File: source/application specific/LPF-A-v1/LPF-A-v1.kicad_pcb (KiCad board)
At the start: 6 copper layers, 32 x 20 mm, 33 parts, among them J1 Conn_01x01_Pin, J2 Conn_01x01_Pin, J3 Conn_01x01_Pin, J4 Conn_01x01_Pin, J5 Conn_01x01_Pin, J6 Conn_01x01_Pin, J7 Conn_01x01_Pin, U1 OPA140, U2 OPA140

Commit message: Updates
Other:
- board text added: "The Manhattan Toolkit LPF-A-v1"
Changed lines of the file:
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@@
 		(layer "Edge.Cuts")
+	)
+	(gr_text "The Manhattan Toolkit\nLPF-A-v1"
+		(at 150 110.25 0)
+		(layer "B.SilkS")
+		(effects
+			(font
+				(size 0.8 0.8)
+				(thickness 0.15)
+				(bold yes)
+			)
+			(justify mirror)
+		)
 	)
 	(gr_text "0V"

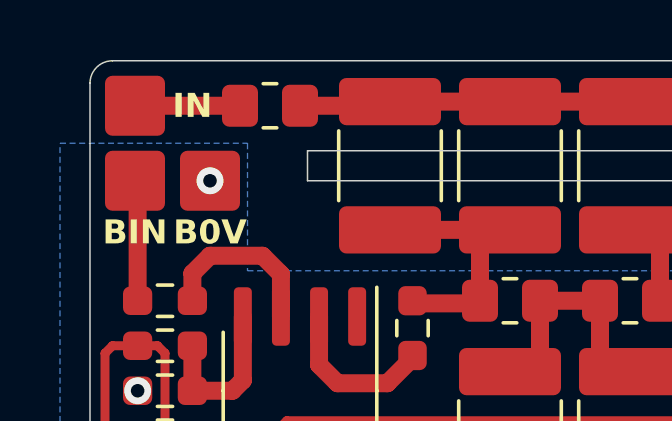
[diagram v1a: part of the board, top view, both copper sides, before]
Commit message: Switched 0805 resistor to 1206
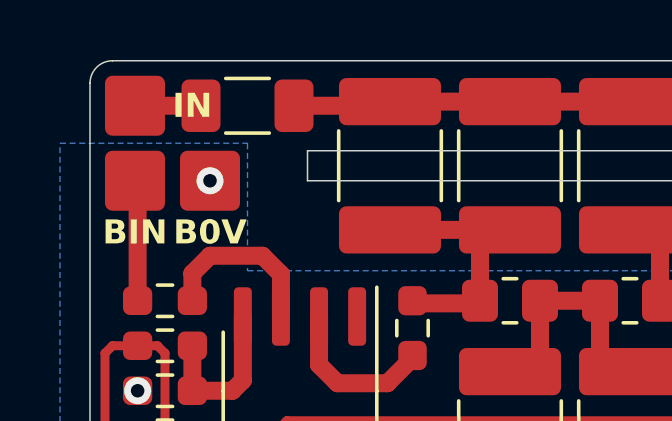
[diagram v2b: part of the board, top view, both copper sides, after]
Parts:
- C7, C8: value 47n -> 10n
- R1: footprint Resistor_SMD:R_0805_2012Metric_Pad1.20x1.40mm_HandSolder -> Resistor_SMD:R_1206_3216Metric_Pad1.30x1.75mm_HandSolder
- R7: value 1k -> 2.2k
- R8: value 100 -> 220
- moved R1 0.75 mm to (139.2, 101.5)
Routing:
- net In: track 3.50 -> 2.20 mm
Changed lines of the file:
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@@
 			)
 		)
-		(property "Value" "47n"
+		(property "Value" "10n"
 			(at 0 1.43 0)
 			(layer "F.Fab")
@@
 			)
 		)
-		(property "Value" "100"
+		(property "Value" "220"
 			(at 0 1.43 0)
 			(layer "F.Fab")
@@
 		)
 	)
-	(footprint "Resistor_SMD:R_0805_2012Metric_Pad1.20x1.40mm_HandSolder"
+	(footprint "Resistor_SMD:R_1206_3216Metric_Pad1.30x1.75mm_HandSolder"
 		(layer "F.Cu")
-		(at 140 101.5)
-		(descr "Resistor SMD 0805 (2012 Metric), square (rectangular) end terminal, IPC_7351 nominal with elongated pad for handsoldering. (Body size source: IPC-SM-782 page 72, https://www.pcb-3d.com/wordpress/wp-content/uploads/ipc-sm-782a_amendment_1_and_2.pdf), generated with kicad-footprint-generator")
+		(at 139.25 101.5)
+		(descr "Resistor SMD 1206 (3216 Metric), square (rectangular) end terminal, IPC_7351 nominal with elongated pad for handsoldering. (Body size source: IPC-SM-782 page 72, https://www.pcb-3d.com/wordpress/wp-content/uploads/ipc-sm-782a_amendment_1_and_2.pdf), generated with kicad-footprint-generator")
 		(tags "resistor handsolder")
 		(property "Reference" "R1"
-			(at 0 -1.65 0)
+			(at 0 -1.82 0)
 			(layer "F.SilkS")
 			(hide yes)
 			(effects
 				(font
-					(size 0.8 0.8)
+					(size 1 1)
 					(thickness 0.15)
 				)
@@
 		)
 		(property "Value" "47k"
-			(at 0 1.65 0)
+			(at 0 1.82 0)
 			(layer "F.Fab")
 			(hide yes)
@@
 			)
 		)
-		(property "Footprint" "Resistor_SMD:R_0805_2012Metric_Pad1.20x1.40mm_HandSolder"
+		(property "Footprint" "Resistor_SMD:R_1206_3216Metric_Pad1.30x1.75mm_HandSolder"
 			(at 0 0 0)
 			(layer "F.Fab")
@@
 		(attr smd)
 		(fp_line
-			(start -0.227064 -0.735)
-			(end 0.227064 -0.735)
+			(start -0.727064 -0.91)
+			(end 0.727064 -0.91)
 			(stroke
 				(width 0.12)
@@
 		)
 		(fp_line
-			(start -0.227064 0.735)
-			(end 0.227064 0.735)
+			(start -0.727064 0.91)
+			(end 0.727064 0.91)
 			(stroke
 				(width 0.12)
@@
 		)
 		(fp_line
-			(start -1.85 -0.95)
-			(end 1.85 -0.95)
+			(start -2.45 -1.12)
+			(end 2.45 -1.12)
 			(stroke
 				(width 0.05)
@@
 		)
 		(fp_line
-			(start -1.85 0.95)
-			(end -1.85 -0.95)
+			(start -2.45 1.12)
+			(end -2.45 -1.12)
 			(stroke
 				(width 0.05)
@@
 		)
 		(fp_line
-			(start 1.85 -0.95)
-			(end 1.85 0.95)
+			(start 2.45 -1.12)
+			(end 2.45 1.12)
 			(stroke
 				(width 0.05)
@@
 		)
 		(fp_line
-			(start 1.85 0.95)
-			(end -1.85 0.95)
+			(start 2.45 1.12)
+			(end -2.45 1.12)
 			(stroke
 				(width 0.05)
@@
 		)
 		(fp_line
-			(start -1 -0.625)
-			(end 1 -0.625)
+			(start -1.6 -0.8)
+			(end 1.6 -0.8)
 			(stroke
 				(width 0.1)
@@
 		)
 		(fp_line
-			(start -1 0.625)
-			(end -1 -0.625)
+			(start -1.6 0.8)
+			(end -1.6 -0.8)
 			(stroke
 				(width 0.1)
@@
 		)
 		(fp_line
-			(start 1 -0.625)
-			(end 1 0.625)
+			(start 1.6 -0.8)
+			(end 1.6 0.8)
 			(stroke
 				(width 0.1)
@@
 		)
 		(fp_line
-			(start 1 0.625)
-			(end -1 0.625)
+			(start 1.6 0.8)
+			(end -1.6 0.8)
 			(stroke
 				(width 0.1)
@@
 			(effects
 				(font
-					(size 0.5 0.5)
-					(thickness 0.08)
+					(size 0.8 0.8)
+					(thickness 0.12)
 				)
 			)
 		)
 		(pad "1" smd roundrect
-			(at -1 0)
-			(size 1.2 1.4)
+			(at -1.55 0)
+			(size 1.3 1.75)
 			(layers "F.Cu" "F.Paste" "F.Mask")
-			(roundrect_rratio 0.208333)
+			(roundrect_rratio 0.192308)
 			(net 11 "In")
 			(pintype "passive")
 		)
 		(pad "2" smd roundrect
-			(at 1 0)
-			(size 1.2 1.4)
+			(at 1.55 0)
+			(size 1.3 1.75)
 			(layers "F.Cu" "F.Paste" "F.Mask")
-			(roundrect_rratio 0.208333)
+			(roundrect_rratio 0.192308)
 			(net 13 "Debug")
 			(pintype "passive")
 		)
-		(model "${KICAD6_3DMODEL_DIR}/Resistor_SMD.3dshapes/R_0805_2012Metric.wrl"
+		(model "${KICAD6_3DMODEL_DIR}/Resistor_SMD.3dshapes/R_1206_3216Metric.wrl"
 			(offset
 				(xyz 0 0 0)
@@
 			)
 		)
-		(property "Value" "47n"
+		(property "Value" "10n"
 			(at 0 1.43 0)
 			(layer "F.Fab")
@@
 			)
 		)
-		(property "Value" "1k"
+		(property "Value" "2.2k"
 			(at 0 1.43 0)
 			(layer "F.Fab")
@@
 	)
 	(segment
-		(start 139 101.5)
+		(start 137.7 101.5)
 		(end 135.5 101.5)
 		(width 0.6)
